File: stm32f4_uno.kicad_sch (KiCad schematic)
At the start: 48 parts, among them J1 Barrel_Jack, J101 Digital/PWM, J102 Power, J103 Analog, J104 Digital/PWM, J106 Ethernet, J107 STM32 GPIO, J108 STM32 GPIO, J109 STM32 GPIO, J110 STM32 GPIO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

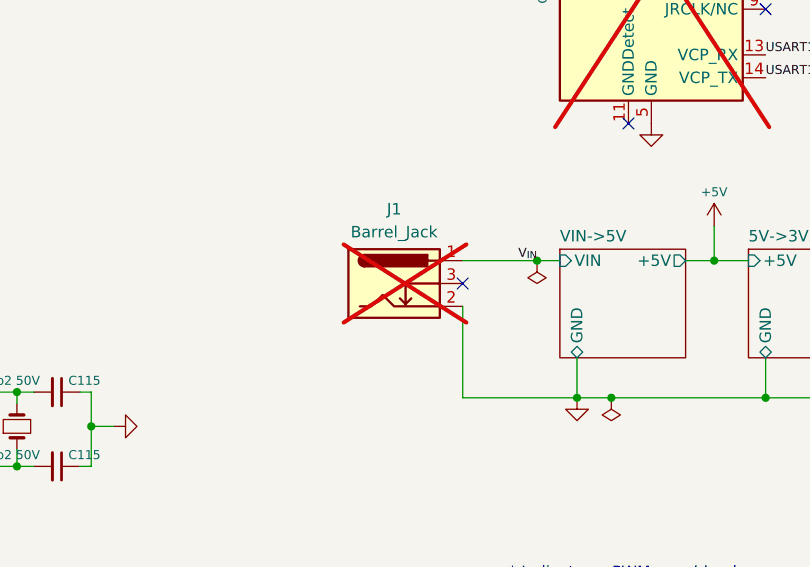
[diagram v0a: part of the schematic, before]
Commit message: Add CUI Devices PJ-102AH 3D model and export PCB 3D model
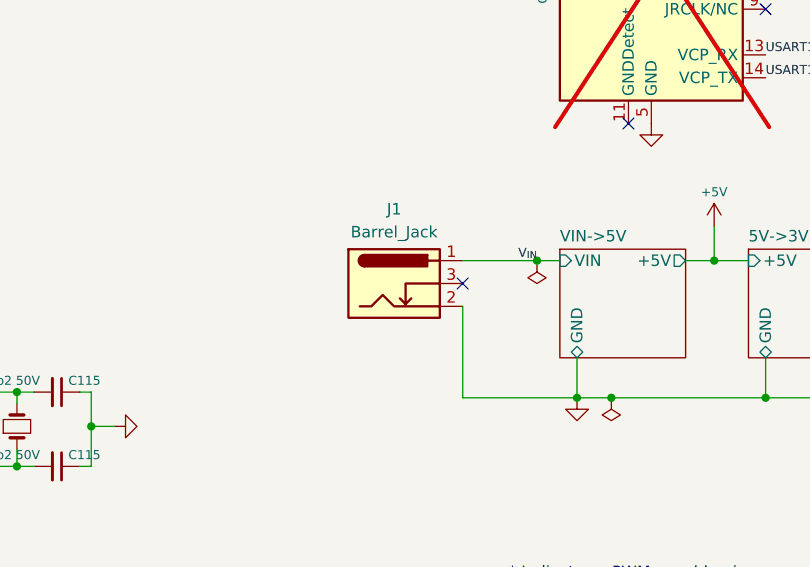
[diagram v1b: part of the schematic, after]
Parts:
- J1: footprint Connector_BarrelJack:BarrelJack_CUI_PJ-102AH_Horizontal -> #Connector:CUI Devices PJ-102AH.pdf; symbol Connector:Barrel_Jack_Switch -> #Connector:CUI Devices PJ-102AH; now fitted
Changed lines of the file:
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@@
     )
   )
-  (symbol (lib_id "Connector:Barrel_Jack_Switch") (at 165.1 147.32 0) (unit 1)
-    (in_bom no) (on_board yes) (dnp yes) (fields_autoplaced)
+  (symbol (lib_id "#Connector:CUI Devices PJ-102AH") (at 165.1 147.32 0) (unit 1)
+    (in_bom no) (on_board yes) (dnp no) (fields_autoplaced)
     (property "Reference" "J1" (at 165.1 139.065 0)
       (effects (font (size 1.27 1.27)))
@@
       (effects (font (size 1.27 1.27)))
     )
-    (property "Footprint" "Connector_BarrelJack:BarrelJack_CUI_PJ-102AH_Horizontal" (at 166.37 148.336 0)
+    (property "Footprint" "#Connector:CUI Devices PJ-102AH.pdf" (at 165.1 154.686 0)
       (effects (font (size 1.27 1.27)) hide)
     )
-    (property "Datasheet" "~" (at 166.37 148.336 0)
+    (property "Datasheet" "${KIPRJMOD}/KiCad-Lib/#Connector.doc/CUI Devices PJ-102AH.pdf" (at 165.1 156.718 0)
       (effects (font (size 1.27 1.27)) hide)
     )

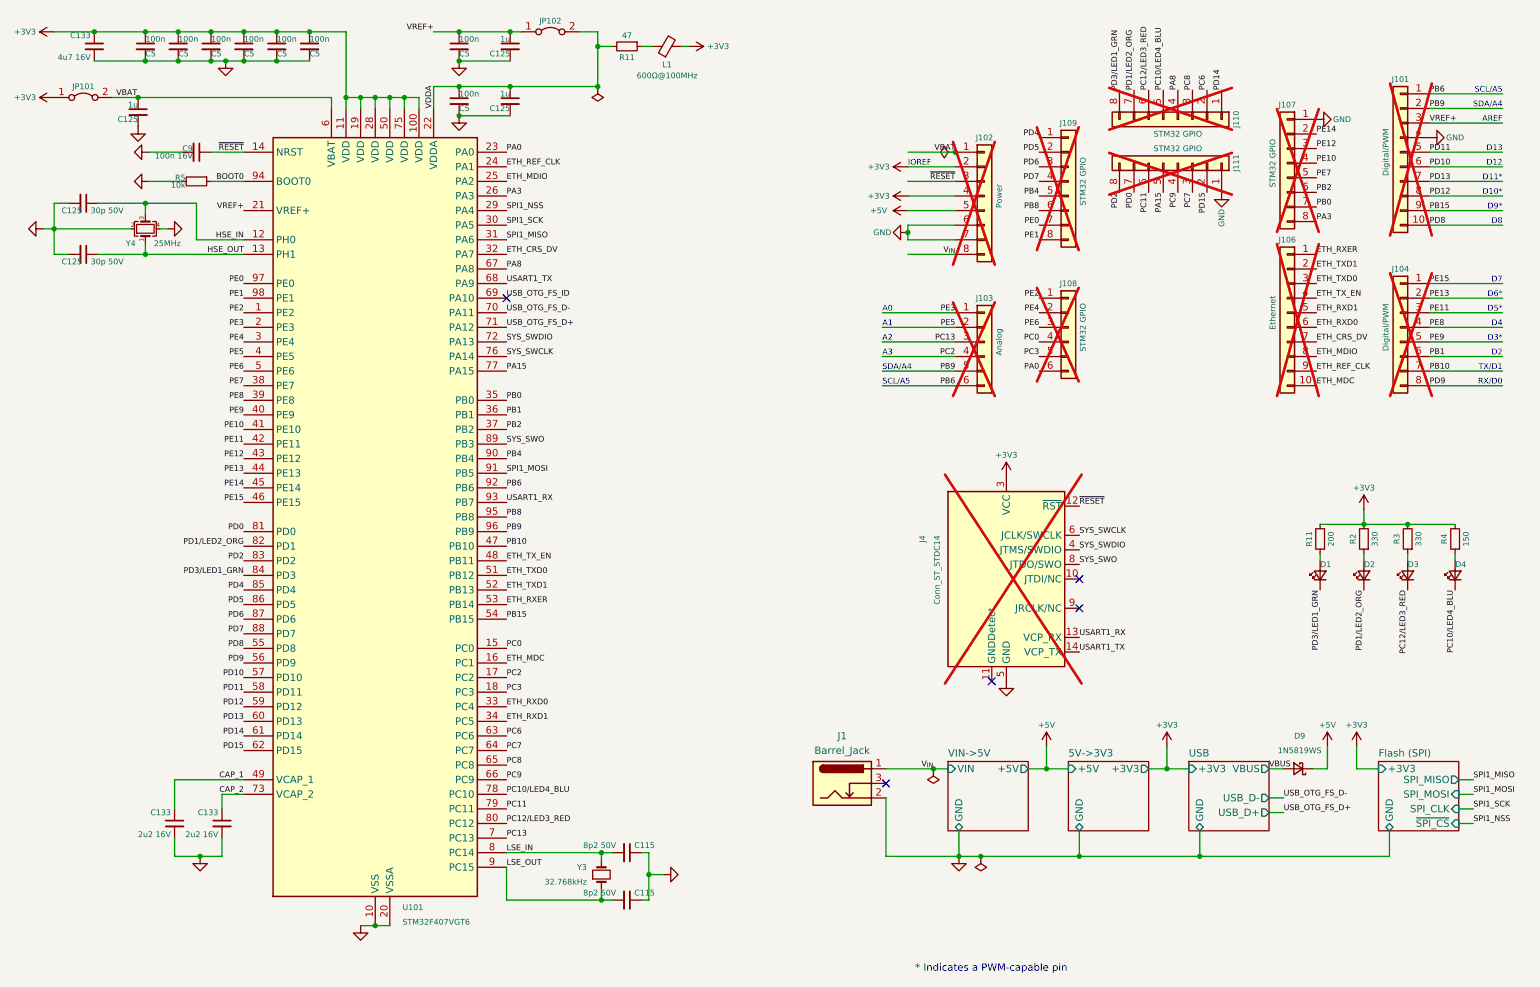
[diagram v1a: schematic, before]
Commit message: Feature/40 v ps (#3)
* WIP

* WIP

* Replaced 5V LDO for a 40V->5V buck converter

* Lock pin sockets
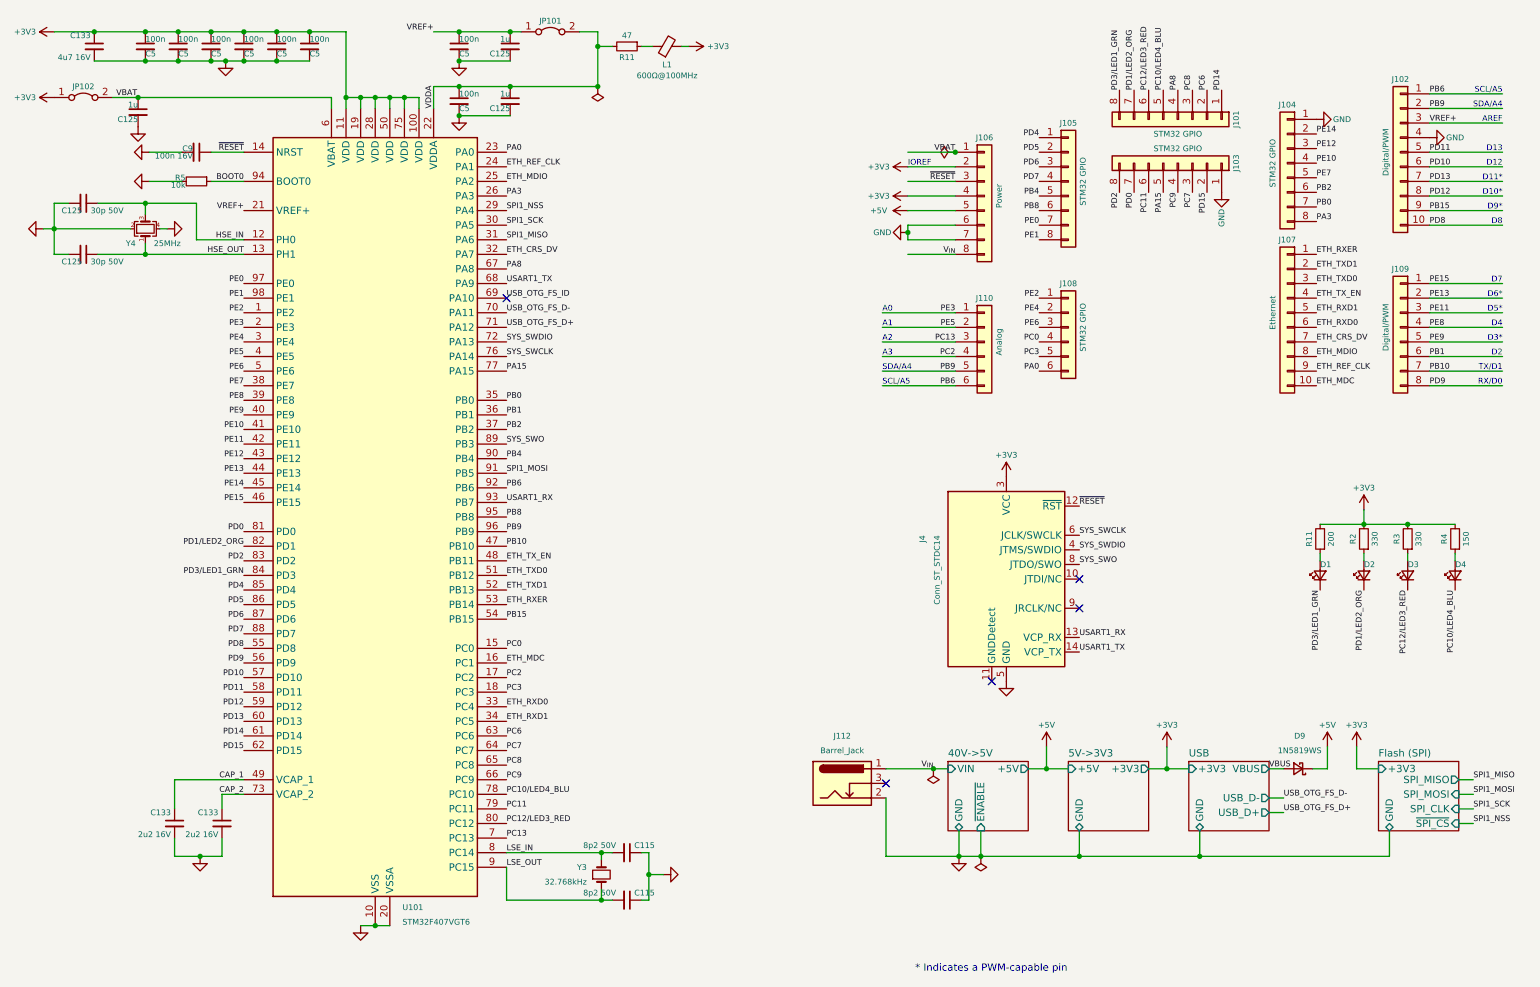
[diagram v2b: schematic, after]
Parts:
- J101: renamed from J110; now fitted
- J102: renamed from J101; now fitted
- J103: renamed from J111; now fitted
- J104: renamed from J107; now fitted
- J105: renamed from J109; now fitted
- J106: renamed from J102; now fitted
- J107: renamed from J106; now fitted
- J108: now fitted
- J109: renamed from J104; now fitted
- J110: renamed from J103; now fitted
- J4: now fitted; now left out of the parts list
- renumbered J1 to J112, JP102 to JP101, JP101 to JP102
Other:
- removed sheet VIN->5V
- added sheet 40V->5V (40V_to_5V.kicad_sch)

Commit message: #2 Add silkscreen texts
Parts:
- added D8: SS210, Diode_SMD:D_SMA, symbol Device:D_Schottky_Small
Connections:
- net V_{IN}: now also D8.1 (K); no longer J112.1
- new net: D8.2 (A), J112.1
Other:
- company: (none) -> easy-smart solution GmbH
- title: (none) -> STM32F4 Uno
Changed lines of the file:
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@@
   (paper "A4")
   (title_block
-    (date "mar. 31 mars 2015")
+    (title "STM32F4 Uno")
+    (date "2023-10-02")
+    (rev "1.0.x-dev")
+    (company "easy-smart solution GmbH")
   )
   (junction (at 227.33 160.02) (diameter 0) (color 0 0 0 0)
@@
     (stroke (width 0) (type solid))
   )
-  (wire (pts (xy 172.72 144.78) (xy 180.975 144.78))
+  (wire (pts (xy 172.72 144.78) (xy 173.99 144.78))
     (stroke (width 0) (type default))
   )
@@
     (stroke (width 0) (type default))
   )
+  (wire (pts (xy 179.07 144.78) (xy 180.975 144.78))
+    (stroke (width 0) (type default))
+  )
   (wire (pts (xy 221.615 140.97) (xy 221.615 144.78))
     (stroke (width 0) (type default))
@@
         )
       )
+    )
+  )
+  (symbol (lib_id "Device:D_Schottky_Small") (at 176.53 144.78 180) (unit 1)
+    (in_bom yes) (on_board yes) (dnp no) (fields_autoplaced)
+    (property "Reference" "D8" (at 176.784 138.43 0)
+      (effects (font (size 0.9 0.9)))
+    )
+    (property "Value" "SS210" (at 176.784 140.97 0)
+      (effects (font (size 0.9 0.9)))
+    )
+    (property "Footprint" "Diode_SMD:D_SMA" (at 176.53 144.78 90)
+      (effects (font (size 1 1)) hide)
+    )
+    (property "Datasheet" "https://datasheet.lcsc.com/lcsc/2304140030_MDD-Microdiode-Electronics--SS210_C14996.pdf" (at 176.53 144.78 90)
+      (effects (font (size 1 1)) hide)
+    )
+    (property "Description" "100V 850mV@2A 2A SMA(DO-214AC)  Schottky Barrier Diodes (SBD) ROHS" (at 176.53 144.78 0)
+      (effects (font (size 1 1)) hide)
+    )
+    (property "Manufacturer" "MDD" (at 176.53 144.78 0)
+      (effects (font (size 1 1)) hide)
+    )
+    (property "Partnumber" "SS210" (at 176.53 144.78 0)
+      (effects (font (size 1 1)) hide)
+    )
+    (property "JLCPCB Part #" "C14996" (at 176.53 144.78 0)
+      (effects (font (size 1 1)) hide)
+    )
+    (property "isBasicPart" "YES" (at 176.53 144.78 0)
+      (effects (font (size 1 1)) hide)
+    )
+    (pin "1")
+    (pin "2")
+    (instances
+      (project "stm32f1_nano"
+        (path "/0d35483a-0b12-46cc-b9f2-896fd6831779"
+          (reference "D8") (unit 1)
+        )
+      )
+      (project "stm32f407vg"
+        (path "/2d452db2-a0cd-4a57-9497-df1dd0591a30/50c2bb91-d0dc-4111-959e-b2cc7ea59413"
+          (reference "D601") (unit 1)
+        )
+      )
+      (project "basicparts"
+        (path "/43a31acf-2604-4bbd-9556-e633c3dff6c4"
+          (reference "D102") (unit 1)
+        )
+      )
+      (project "stm32f4_uno"
+        (path "/e63e39d7-6ac0-4ffd-8aa3-1841a4541b55"
+          (reference "D106") (unit 1)
+        )
+      )
